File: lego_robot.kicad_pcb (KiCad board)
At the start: 2 copper layers, 9 parts, among them J1 Motor_Connector, J2 Motor_Connector, J3 Motor_Connector, U3 L80-M39, U4 STM32-NUCLEO-F446RE, U5 ICM-20948, U6 BD65496MUV, U7 BD65496MUV, U8 BD65496MUV

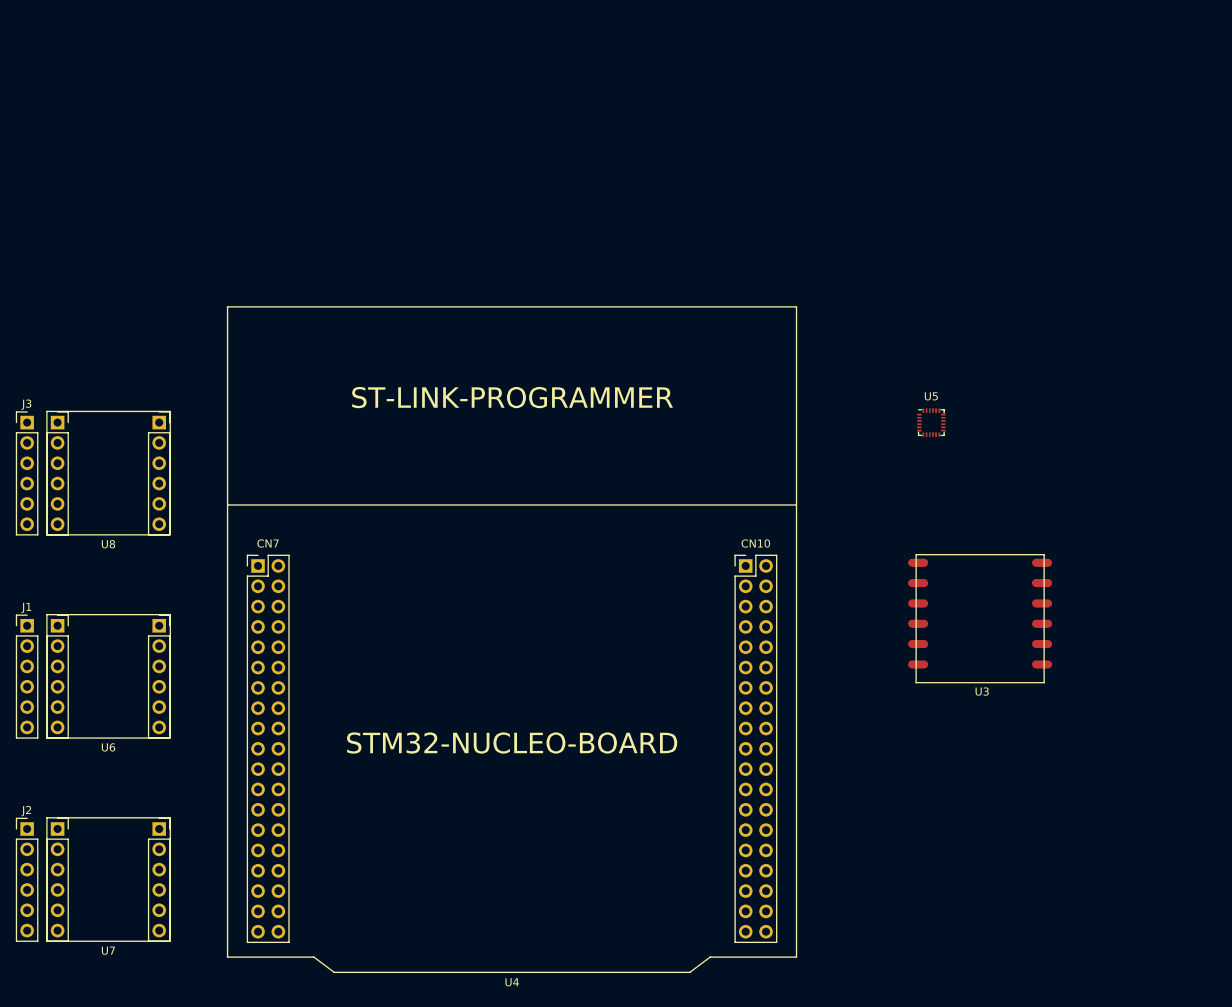
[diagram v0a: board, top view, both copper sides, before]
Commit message: Preliminary PCB edge cuts and placements
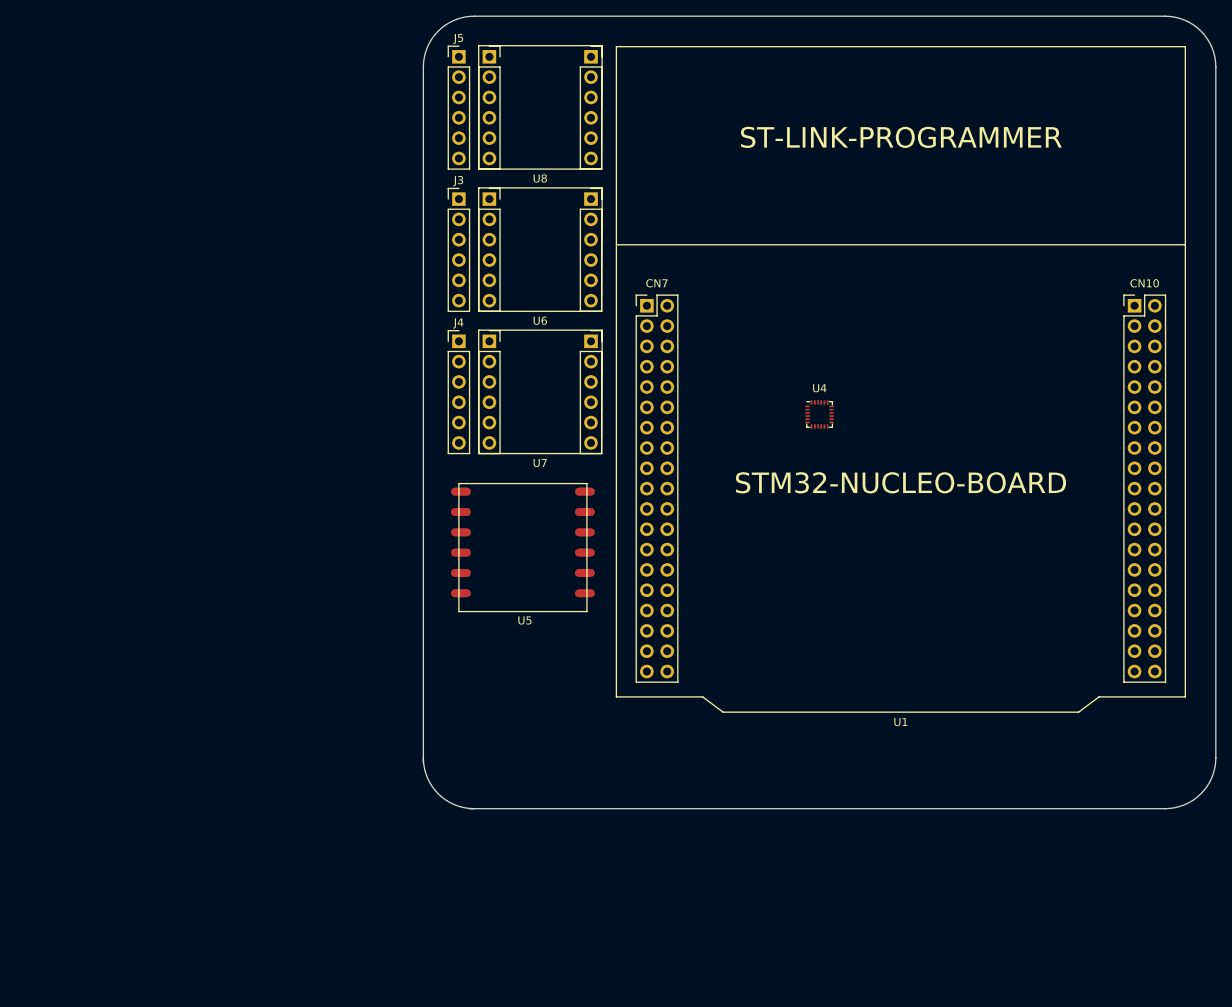
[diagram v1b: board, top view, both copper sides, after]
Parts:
- moved U7 81.4 mm to (103.5, 85.1)
- moved J4 81.4 mm to (93.3, 78.7)
- moved J3 75.9 mm to (93.3, 61.0)
- moved U6 75.9 mm to (103.5, 67.3)
- moved J5 70.7 mm to (93.3, 43.2)
- moved U8 70.7 mm to (103.5, 49.5)
- moved U1 58.5 mm to (148.6, 97.2)
- moved U5 57.8 mm to (101.6, 105.4)
- moved U4 14.0 mm to (138.4, 87.9)
- renumbered J1 to J3, J2 to J4, J3 to J5, U4 to U1, U5 to U4, U3 to U5
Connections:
- net Net-(U4-Pad18) renamed /LOGIC_5V
- net Net-(U6-Pad7) renamed /~MOTOR1_PS
- net Net-(U7-Pad7) renamed /~MOTOR2_PS
- net Net-(U8-Pad7) renamed /~MOTOR3_PS
- J3 pad 3: Net-(J1-Pad3) -> /LOGIC_GND
- J3 pad 4: Net-(J1-Pad4) -> /LOGIC_3V3
- J4 pad 3: Net-(J2-Pad3) -> /LOGIC_GND
- J4 pad 4: Net-(J2-Pad4) -> /LOGIC_3V3
- J5 pad 3: Net-(J3-Pad3) -> /LOGIC_GND
- J5 pad 4: Net-(J3-Pad4) -> /LOGIC_3V3
- U1 pad 1: Net-(U4-Pad1) (its old number) -> /GPS_UART_RX
- U1 pad 16: Net-(U4-Pad16) (its old number) -> /LOGIC_3V3
- U1 pad 19: Net-(U4-Pad19) (its old number) -> /LOGIC_GND
- U1 pad 2: Net-(U4-Pad2) (its old number) -> /GPS_UART_TX
- U1 pad 20: Net-(U4-Pad20) -> /LOGIC_GND
- U1 pad 22: Net-(U4-Pad22) (its old number) -> /LOGIC_GND
- U1 pad 3: Net-(U4-Pad3) (its old number) -> /GPS_RESET
- U1 pad 47: Net-(U4-Pad47) -> /LOGIC_GND
- U1 pad 58: Net-(U4-Pad58) -> /LOGIC_GND
- U1 pad 6: Net-(U4-Pad6) (its old number) -> /VBAT_REG
- U1 pad 70: Net-(U4-Pad70) -> /LOGIC_GND
- U1 pad 8: Net-(U4-Pad8) -> /LOGIC_GND
- U4 pad 13: Net-(U5-Pad13) -> /LOGIC_3V3
- U4 pad 18: Net-(U5-Pad18) -> GND
- U4 pad 20: Net-(U5-Pad18) -> GND
- U4 pad 8: Net-(U5-Pad8) (its old number) -> /LOGIC_3V3
- U5 pad 12: GND -> /LOGIC_GND
- U5 pad 3: GND -> /LOGIC_GND
- U5 pad 4: Net-(U3-Pad4) -> /LOGIC_3V3
- U5 pad 5: Net-(U3-Pad5) -> /LOGIC_3V3
- U6 pad 1: Net-(U6-Pad1) -> /LOGIC_3V3
- U6 pad 12: Net-(U6-Pad12) -> /MOTOR_MODE
- U6 pad 2: Net-(U6-Pad2) -> /MOTOR_GND
- U6 pad 5: Net-(U6-Pad5) -> /MOTOR_VIN
- U6 pad 6: Net-(U6-Pad6) -> /LOGIC_GND
- U6 pad 8: Net-(U6-Pad8) -> /MOTOR_TR1
- U6 pad 9: Net-(U6-Pad9) -> /MOTOR_TR2
- U7 pad 1: Net-(U7-Pad1) -> /LOGIC_3V3
- U7 pad 12: Net-(U7-Pad12) -> /MOTOR_MODE
- U7 pad 2: Net-(U7-Pad2) -> /MOTOR_GND
- U7 pad 5: Net-(U7-Pad5) -> /MOTOR_VIN
- U7 pad 6: Net-(U7-Pad6) -> /LOGIC_GND
- U7 pad 8: Net-(U7-Pad8) -> /MOTOR_TR1
- U7 pad 9: Net-(U7-Pad9) -> /MOTOR_TR2
- U8 pad 1: Net-(U8-Pad1) -> /LOGIC_3V3
- U8 pad 12: Net-(U8-Pad12) -> /MOTOR_MODE
- U8 pad 2: Net-(U8-Pad2) -> /MOTOR_GND
- U8 pad 5: Net-(U8-Pad5) -> /MOTOR_VIN
- U8 pad 6: Net-(U8-Pad6) -> /LOGIC_GND
- U8 pad 8: Net-(U8-Pad8) -> /MOTOR_TR1
- U8 pad 9: Net-(U8-Pad9) -> /MOTOR_TR2
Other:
- board outline added: 99.1 x 99.1 mm

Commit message: mostly done
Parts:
- moved U4 47.9 mm to (100.1, 116.6)
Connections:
- net /~MOTOR1_PS renamed /~{MOTOR1_PS}
- net /~MOTOR2_PS renamed /~{MOTOR2_PS}
- net /~MOTOR3_PS renamed /~{MOTOR3_PS}
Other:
- net class Default removed
